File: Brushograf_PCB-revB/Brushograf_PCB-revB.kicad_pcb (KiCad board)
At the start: 2 copper layers, 230 x 85 mm, 72 parts, among them J1 Conn_01x05_Socket, J12 USB-C PD in, J13 Pendant, J2 Conn_01x05_Socket, J3 Conn_01x05_Socket, J8 SD_CARD_MICRO_AMPHENOL_114008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, SW1 ESP POWER, SW2 SW_Lever_1P2T_NKK_GW12LxH, U1 ULN2003A, U2 ULN2003A, U3 ULN2003A, U4 ESP32-DevKitC, U6 CH224K, U7 TPS54202, U8 TPS54202

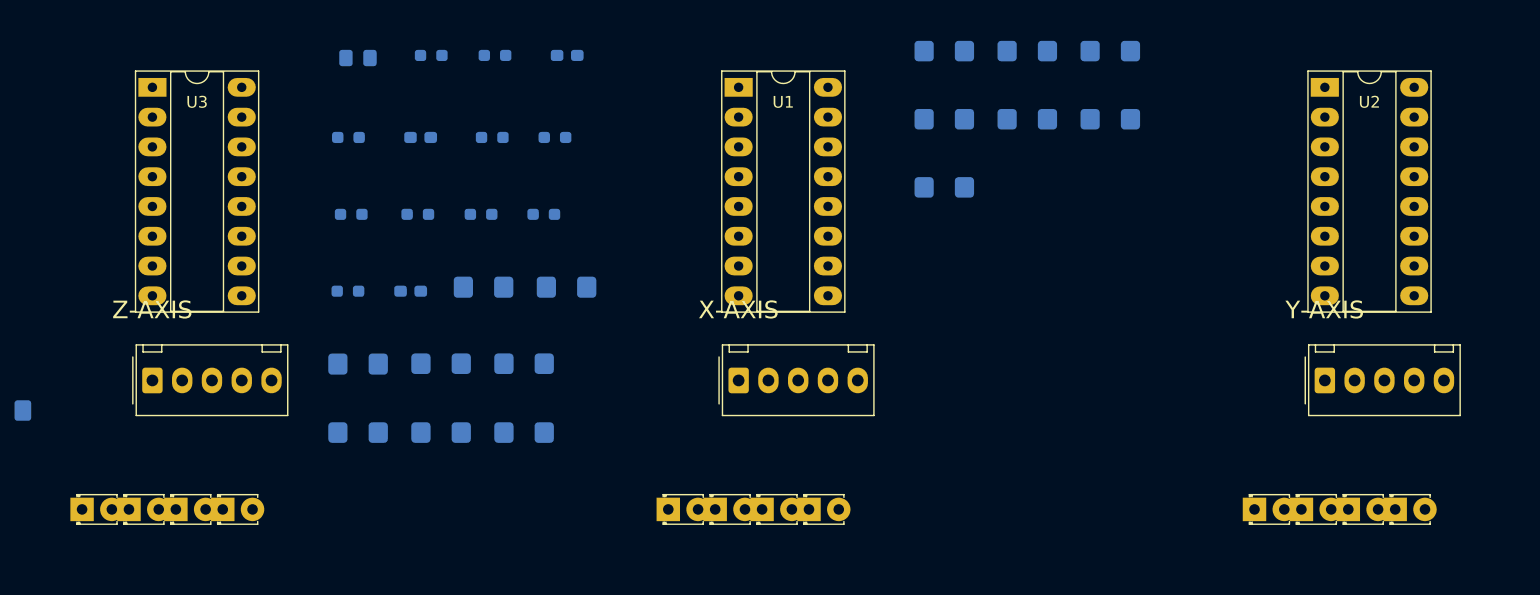
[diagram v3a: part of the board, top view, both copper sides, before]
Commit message: Mathematically center align Motor LEDs, Drivers, and Connectors
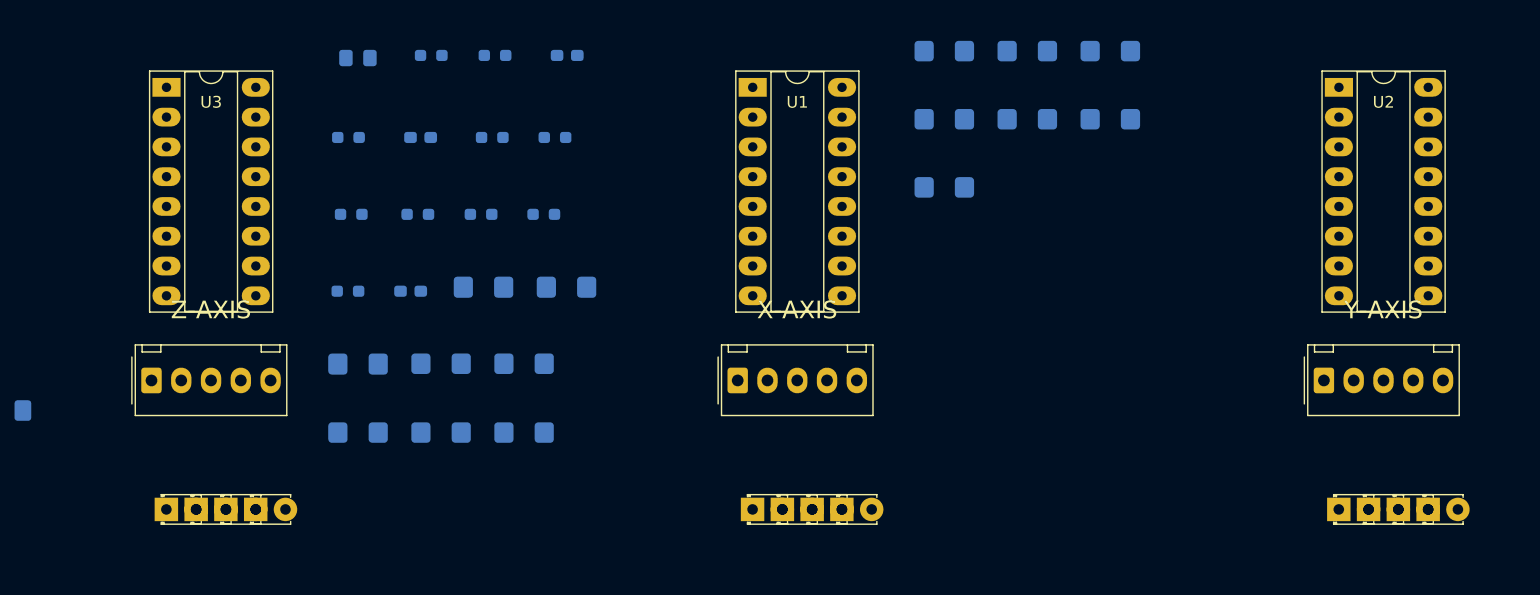
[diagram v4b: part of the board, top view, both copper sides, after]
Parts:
- moved D1 7.19 mm to (171.2, 86.0)
- moved D5 7.19 mm to (221.2, 86.0)
- moved D9 7.19 mm to (121.2, 86.0)
- moved D10 5.73 mm to (123.7, 86.0)
- moved D2 5.73 mm to (173.7, 86.0)
- moved D6 5.73 mm to (223.7, 86.0)
- moved D3 4.27 mm to (176.3, 86.0)
- moved D7 4.27 mm to (226.3, 86.0)
- moved D11 4.27 mm to (126.3, 86.0)
- moved D12 2.81 mm to (128.8, 86.0)
- moved D4 2.81 mm to (178.8, 86.0)
- moved D8 2.81 mm to (228.8, 86.0)
- moved U3 1.20 mm to (121.2, 50.0)
- moved U1 1.20 mm to (171.2, 50.0)
- moved U2 1.20 mm to (221.2, 50.0)
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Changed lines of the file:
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@@
 	(footprint "009_Brushograph:LED_D1.8mm_Brushograf"
 		(layer "F.Cu")
-		(at 168 86)
+		(at 173.73 86)
 		(descr "LED, Round, Rectangular, size 3.3x2.4mm, diameter 1.8mm, 2 pins, generated by kicad-footprint-generator")
 		(tags "LED")
@@
 	(footprint "009_Brushograph:LED_D1.8mm_Brushograf"
 		(layer "F.Cu")
-		(at 122 86)
+		(at 126.27 86)
 		(descr "LED, Round, Rectangular, size 3.3x2.4mm, diameter 1.8mm, 2 pins, generated by kicad-footprint-generator")
 		(tags "LED")
@@
 	(footprint "009_Brushograph:Molex_1x05_P2.54mm_Brushograf"
 		(layer "F.Cu")
-		(at 120 75)
+		(at 119.92 75)
 		(descr "Molex KK-254 Interconnect System, old/engineering part number: AE-6410-05A example for new part number: 22-27-2051, 5 Pins (http://www.molex.com/pdm_docs/sd/022272021_sd.pdf), generated with kicad-footprint-generator")
 		(tags "connector Molex KK-254 vertical")
@@
 	(footprint "009_Brushograph:LED_D1.8mm_Brushograf"
 		(layer "F.Cu")
-		(at 114 86)
+		(at 121.19 86)
 		(descr "LED, Round, Rectangular, size 3.3x2.4mm, diameter 1.8mm, 2 pins, generated by kicad-footprint-generator")
 		(tags "LED")
@@
 	(footprint "009_Brushograph:DIP-16_W7.62mm_Socket_Brushograf"
 		(layer "F.Cu")
-		(at 120 50)
+		(at 121.2 50)
 		(descr "16-lead though-hole mounted DIP package, row spacing 7.62 mm (300 mils), Socket, LongPads")
 		(tags "THT DIP DIL PDIP 2.54mm 7.62mm 300mil Socket LongPads")
@@
 	(footprint "009_Brushograph:LED_D1.8mm_Brushograf"
 		(layer "F.Cu")
-		(at 222 86)
+		(at 226.27 86)
 		(descr "LED, Round, Rectangular, size 3.3x2.4mm, diameter 1.8mm, 2 pins, generated by kicad-footprint-generator")
 		(tags "LED")
@@
 	(footprint "009_Brushograph:LED_D1.8mm_Brushograf"
 		(layer "F.Cu")
-		(at 126 86)
+		(at 128.81 86)
 		(descr "LED, Round, Rectangular, size 3.3x2.4mm, diameter 1.8mm, 2 pins, generated by kicad-footprint-generator")
 		(tags "LED")
@@
 	(footprint "009_Brushograph:LED_D1.8mm_Brushograf"
 		(layer "F.Cu")
-		(at 118 86)
+		(at 123.73 86)
 		(descr "LED, Round, Rectangular, size 3.3x2.4mm, diameter 1.8mm, 2 pins, generated by kicad-footprint-generator")
 		(tags "LED")
@@
 	(footprint "009_Brushograph:LED_D1.8mm_Brushograf"
 		(layer "F.Cu")
-		(at 218 86)
+		(at 223.73 86)
 		(descr "LED, Round, Rectangular, size 3.3x2.4mm, diameter 1.8mm, 2 pins, generated by kicad-footprint-generator")
 		(tags "LED")
@@
 	(footprint "009_Brushograph:LED_D1.8mm_Brushograf"
 		(layer "F.Cu")
-		(at 172 86)
+		(at 176.27 86)
 		(descr "LED, Round, Rectangular, size 3.3x2.4mm, diameter 1.8mm, 2 pins, generated by kicad-footprint-generator")
 		(tags "LED")
@@
 	(footprint "009_Brushograph:DIP-16_W7.62mm_Socket_Brushograf"
 		(layer "F.Cu")
-		(at 220 50)
+		(at 221.2 50)
 		(descr "16-lead though-hole mounted DIP package, row spacing 7.62 mm (300 mils), Socket, LongPads")
 		(tags "THT DIP DIL PDIP 2.54mm 7.62mm 300mil Socket LongPads")
@@
 	(footprint "009_Brushograph:LED_D1.8mm_Brushograf"
 		(layer "F.Cu")
-		(at 214 86)
+		(at 221.19 86)
 		(descr "LED, Round, Rectangular, size 3.3x2.4mm, diameter 1.8mm, 2 pins, generated by kicad-footprint-generator")
 		(tags "LED")
@@
 	(footprint "009_Brushograph:Molex_1x05_P2.54mm_Brushograf"
 		(layer "F.Cu")
-		(at 220 75)
+		(at 219.92 75)
 		(descr "Molex KK-254 Interconnect System, old/engineering part number: AE-6410-05A example for new part number: 22-27-2051, 5 Pins (http://www.molex.com/pdm_docs/sd/022272021_sd.pdf), generated with kicad-footprint-generator")
 		(tags "connector Molex KK-254 vertical")
@@
 	(footprint "009_Brushograph:LED_D1.8mm_Brushograf"
 		(layer "F.Cu")
-		(at 176 86)
+		(at 178.81 86)
 		(descr "LED, Round, Rectangular, size 3.3x2.4mm, diameter 1.8mm, 2 pins, generated by kicad-footprint-generator")
 		(tags "LED")
@@
 	(footprint "009_Brushograph:Molex_1x05_P2.54mm_Brushograf"
 		(layer "F.Cu")
-		(at 170 75)
+		(at 169.92 75)
 		(descr "Molex KK-254 Interconnect System, old/engineering part number: AE-6410-05A example for new part number: 22-27-2051, 5 Pins (http://www.molex.com/pdm_docs/sd/022272021_sd.pdf), generated with kicad-footprint-generator")
 		(tags "connector Molex KK-254 vertical")
@@
 	(footprint "009_Brushograph:LED_D1.8mm_Brushograf"
 		(layer "F.Cu")
-		(at 164 86)
+		(at 171.19 86)
 		(descr "LED, Round, Rectangular, size 3.3x2.4mm, diameter 1.8mm, 2 pins, generated by kicad-footprint-generator")
 		(tags "LED")
@@
 	(footprint "009_Brushograph:DIP-16_W7.62mm_Socket_Brushograf"
 		(layer "F.Cu")
-		(at 170 50)
+		(at 171.2 50)
 		(descr "16-lead though-hole mounted DIP package, row spacing 7.62 mm (300 mils), Socket, LongPads")
 		(tags "THT DIP DIL PDIP 2.54mm 7.62mm 300mil Socket LongPads")
@@
 	(footprint "009_Brushograph:LED_D1.8mm_Brushograf"
 		(layer "F.Cu")
-		(at 226 86)
+		(at 228.81 86)
 		(descr "LED, Round, Rectangular, size 3.3x2.4mm, diameter 1.8mm, 2 pins, generated by kicad-footprint-generator")
 		(tags "LED")
@@
 	)
 	(gr_text "Z-AXIS"
-		(at 120 69 0)
+		(at 125 69 0)
 		(layer "F.SilkS")
 		(effects
@@
 	)
 	(gr_text "X-AXIS"
-		(at 170 69 0)
+		(at 175 69 0)
 		(layer "F.SilkS")
 		(effects
@@
 	)
 	(gr_text "Y-AXIS"
-		(at 220 69 0)
+		(at 225 69 0)
 		(layer "F.SilkS")
 		(effects

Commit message: Ultra-wide strip form factor, USB-C facing up and edge-aligned
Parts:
- moved R23 76.1 mm to (66.7, 65.6)
- moved R29 76.1 mm to (72.1, 65.6)
- moved R30 76.1 mm to (77.5, 65.6)
- moved U8 70.9 mm to (140.9, 38.2)
- moved D19 68.7 mm to (138.4, 50.3)
- moved D11 54.2 mm to (176.3, 65.0)
- moved D12 54.2 mm to (178.8, 65.0)
- moved D9 54.2 mm to (171.2, 65.0)
- moved D10 54.2 mm to (173.7, 65.0)
- moved C9 53.9 mm to (88.2, 65.6)
- moved R25 53.9 mm to (82.8, 65.6)
- moved C2 53.9 mm to (101.5, 65.3)
- moved C3 53.9 mm to (94.4, 65.3)
- moved J3 53.9 mm to (169.9, 55.0)
- moved U3 53.9 mm to (171.2, 30.0)
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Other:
- board size 230 x 85 mm -> 265 x 65 mm

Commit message: Optimize form factor to highly compact 200x55mm strip layout
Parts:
- moved R1 162.5 mm to (43.8, 58.6)
- moved R3 162.5 mm to (36.7, 58.6)
- moved R5 162.5 mm to (29.6, 58.6)
- moved R8 162.5 mm to (22.5, 58.6)
- moved R7 133.7 mm to (36.7, 52.8)
- moved R10 133.7 mm to (43.8, 52.8)
- moved R4 133.7 mm to (29.6, 52.8)
- moved R9 122.0 mm to (22.5, 52.8)
- moved R26 119.2 mm to (27.3, 34.3)
- moved R31 119.2 mm to (21.7, 34.3)
- moved R11 94.8 mm to (43.8, 47.0)
- moved R12 94.8 mm to (29.6, 47.0)
- moved R6 94.8 mm to (36.7, 47.0)
- moved R2 94.8 mm to (22.5, 47.0)
- moved C16 76.5 mm to (177.3, 14.3)
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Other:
- board size 265 x 65 mm -> 200 x 55 mm

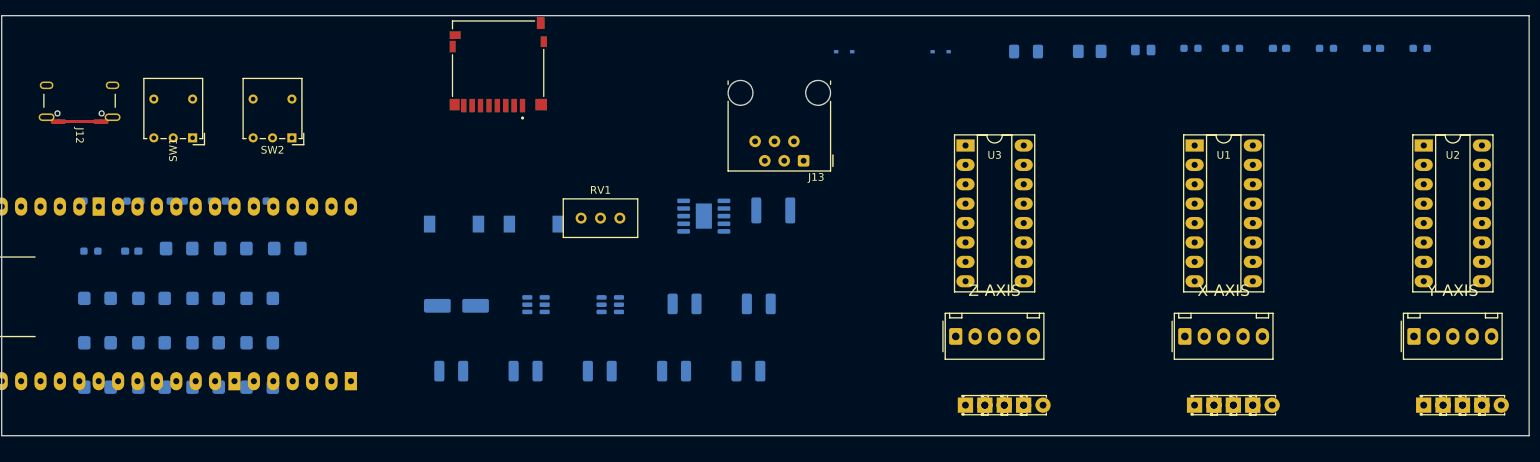
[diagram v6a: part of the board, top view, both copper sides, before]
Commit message: Auto-route compact strip layout via FreeRouting
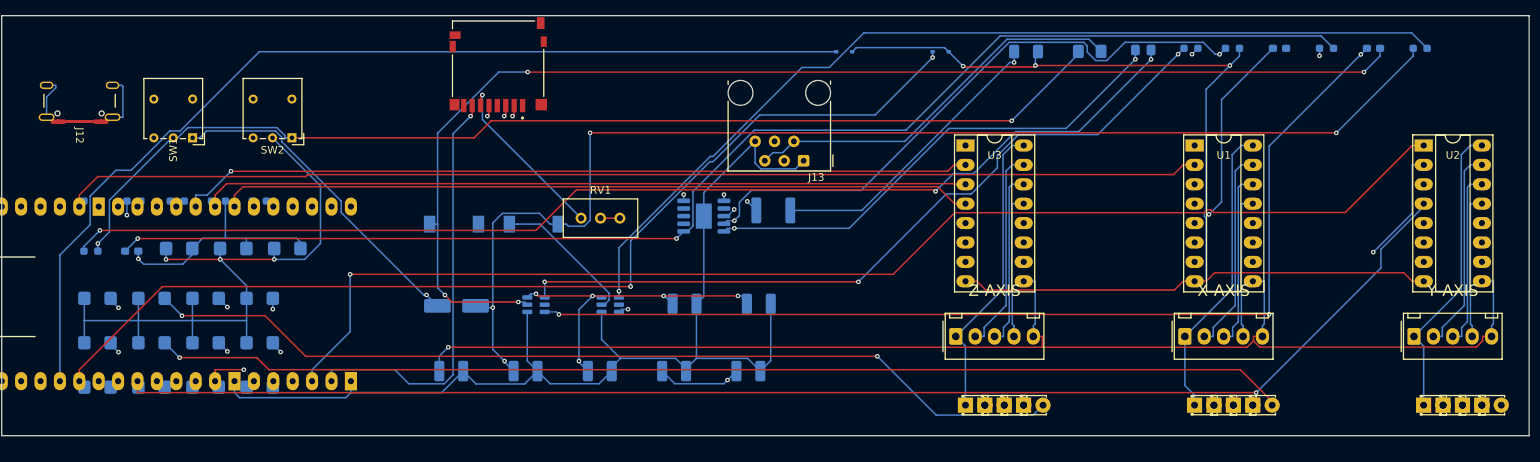
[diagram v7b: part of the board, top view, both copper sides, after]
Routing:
- net GND: track 0.00 -> 361.7 mm, vias 0 -> 5
- net 5V: track 0.00 -> 265.5 mm, vias 0 -> 4
- net IN4_U2: track 0.00 -> 181.8 mm, vias 0 -> 1
- net Net-(U6-VDD): track 0.00 -> 173.2 mm, vias 0 -> 2
- net IN1_U2: track 0.00 -> 163.9 mm, vias 0 -> 1
- net Net-(U7-SW): track 0.00 -> 162.5 mm, vias 0 -> 4
- net 5V_LOGIC: track 0.00 -> 161.5 mm, vias 0 -> 4
- net Net-(D17-A): track 0.00 -> 151.9 mm, vias 0 -> 3
- net IN2_U1: track 0.00 -> 149.2 mm
- net Net-(D4-A): track 0.00 -> 148.7 mm, vias 0 -> 1
- net 5V_SYS: track 0.00 -> 143.7 mm, vias 0 -> 2
- net Net-(U7-BOOT): track 0.00 -> 135.1 mm, vias 0 -> 3
- net PEND_TX: track 0.00 -> 134.4 mm, vias 0 -> 2
- net PEND_RX: track 0.00 -> 131.4 mm
- net Net-(U8-FB): track 0.00 -> 124.8 mm, vias 0 -> 1
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
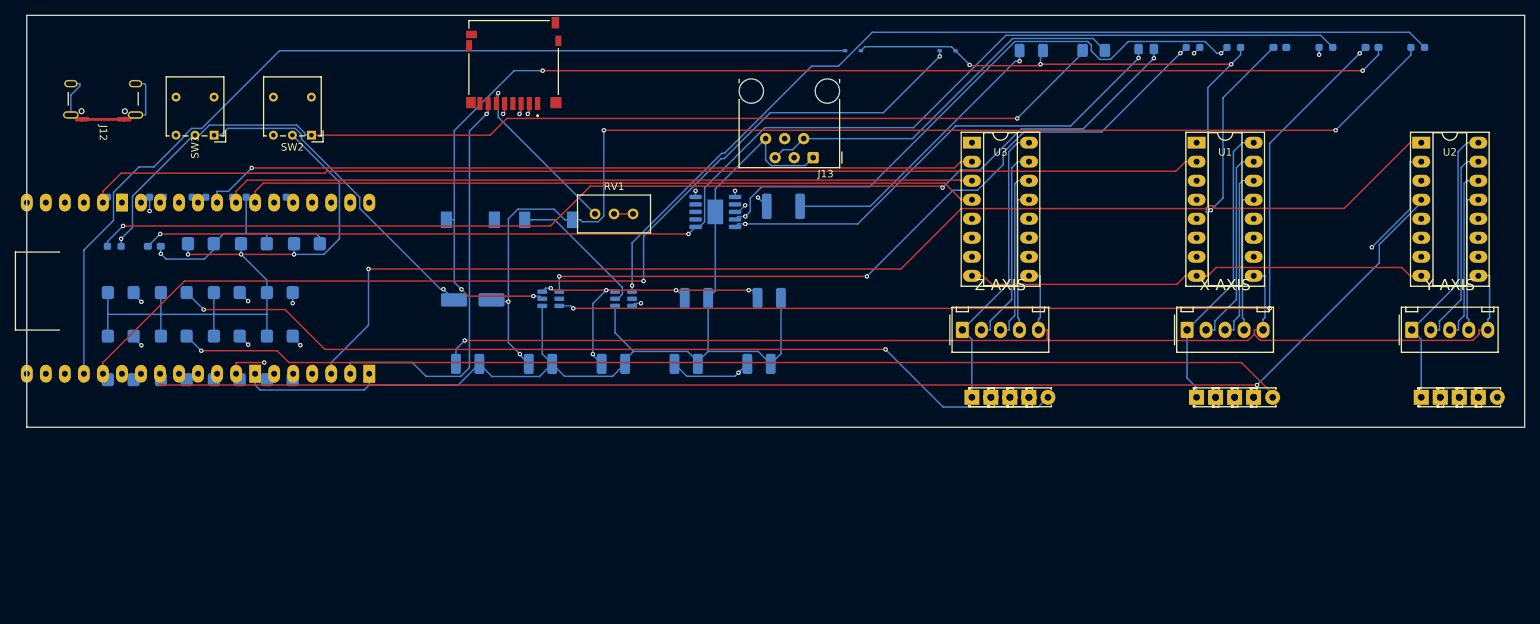
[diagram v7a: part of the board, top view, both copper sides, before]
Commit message: Shift motors left symmetrically, add piezo pickup headers
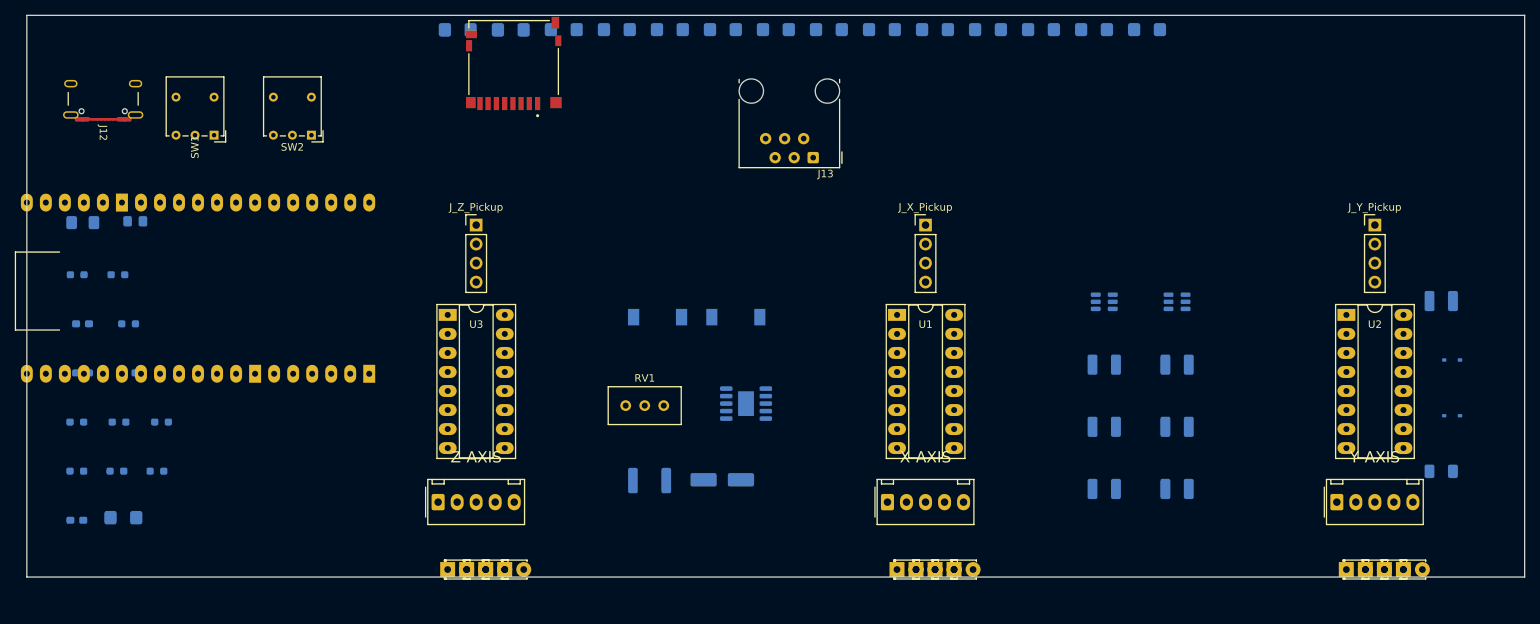
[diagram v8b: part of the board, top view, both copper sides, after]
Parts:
- added J_X_Pickup: PinHeader_1x04_P2.54mm_Vertical, PinHeader_1x04_P2.54mm_Vertical, F.Cu at (130.0, 38.0)
- added J_Y_Pickup: PinHeader_1x04_P2.54mm_Vertical, PinHeader_1x04_P2.54mm_Vertical, F.Cu at (190.0, 38.0)
- added J_Z_Pickup: PinHeader_1x04_P2.54mm_Vertical, PinHeader_1x04_P2.54mm_Vertical, F.Cu at (70.0, 38.0)
- moved C12 177.6 mm to (17.4, 57.7)
- moved R28 177.6 mm to (23.5, 57.7)
- moved R22 164.1 mm to (23.6, 51.2)
- moved C16 164.1 mm to (17.4, 51.2)
- moved R27 152.1 mm to (16.7, 44.6)
- moved R24 152.1 mm to (22.2, 44.6)
- moved D17 136.9 mm to (24.5, 37.5)
- moved F2 136.9 mm to (17.5, 37.7)
- moved R1 124.9 mm to (159.6, 11.9)
- moved R8 124.9 mm to (138.3, 11.9)
- moved R3 124.9 mm to (152.5, 11.9)
- moved R5 124.9 mm to (145.4, 11.9)
- moved R7 96.6 mm to (124.2, 11.9)
- moved R4 96.6 mm to (117.1, 11.9)
- moved R9 96.6 mm to (110.0, 11.9)
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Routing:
- net GND: track 361.7 -> 0.00 mm, vias 5 -> 0
- net 5V: track 265.5 -> 0.00 mm, vias 4 -> 0
- net IN4_U2: track 181.8 -> 0.00 mm, vias 1 -> 0
- net Net-(U6-VDD): track 173.2 -> 0.00 mm, vias 2 -> 0
- net IN1_U2: track 163.9 -> 0.00 mm, vias 1 -> 0
- net Net-(U7-SW): track 162.5 -> 0.00 mm, vias 4 -> 0
- net 5V_LOGIC: track 161.5 -> 0.00 mm, vias 4 -> 0
- net Net-(D17-A): track 151.9 -> 0.00 mm, vias 3 -> 0
- net IN2_U1: track 149.2 -> 0.00 mm
- net Net-(D4-A): track 148.7 -> 0.00 mm, vias 1 -> 0
- net 5V_SYS: track 143.7 -> 0.00 mm, vias 2 -> 0
- net Net-(U7-BOOT): track 135.1 -> 0.00 mm, vias 3 -> 0
- net PEND_TX: track 134.4 -> 0.00 mm, vias 2 -> 0
- net PEND_RX: track 131.4 -> 0.00 mm
- net Net-(U8-FB): track 124.8 -> 0.00 mm, vias 1 -> 0
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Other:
- board size 200 x 55 mm -> 200 x 75 mm
